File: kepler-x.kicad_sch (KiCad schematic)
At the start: 108 parts, among them IC1 SLG46826G, J1 HDMI_C_1.3, J2 Conn_01x02_Male, J3 MIDI OUT, J4 RasPI_IO_Header_B+, J5 AudioJack3, J6 MIDI IN, J7 Conn_01x02_Male, J8 Conn_02x07_Odd_Even, J9 Conn_01x02_Male, Q1 Q_PNP_BEC, Q2 Q_PNP_BEC, Q3 Q_NPN_BEC, Q4 Q_NPN_BEC, Q5 Q_NPN_BEC, Q6 Q_NPN_BEC, SW1 SWITCH_INV, SW2 SWITCH_INV, U1 Bus-X68000-ext, U10 74LVTH162245, U11 WM8804GEDS{slash}RV, U12 TC7MPB9307F, U13 TC7MPB9307F, U14 P0082(DE0-NANO), U15 PLR135-T10, U16 PCM5102, U17 LM1117GS-3.3, U18 H11L1, U2 LM1117GS-3.3, U3 INA3221, U4 74AHC16374, U5 74AHC16374, U6 74AHC16374, U7 74AHC16374, U8 74AHC16374, U9 74AHC16374, X1 ASV-24.576MHz, Y1 12MHz

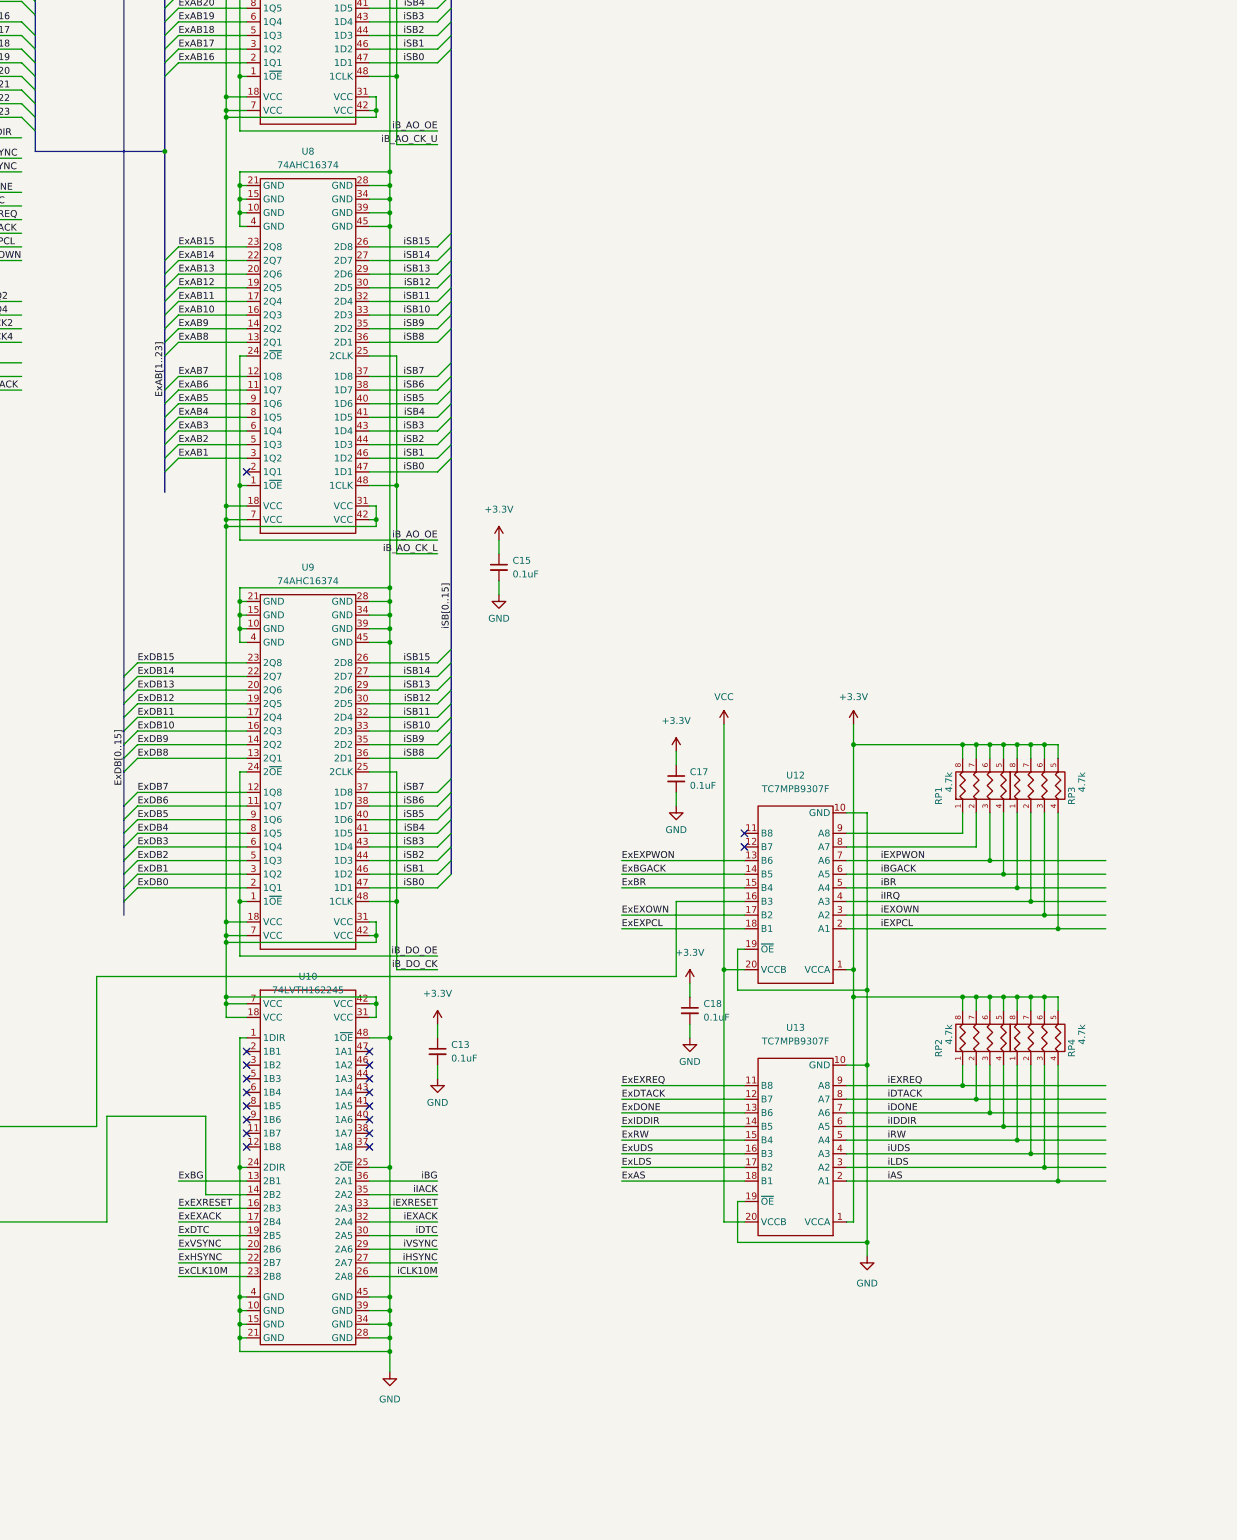
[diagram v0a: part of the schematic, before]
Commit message: Fixed the board can accept TC7MPB9307FT or TC7MPB9307FK.
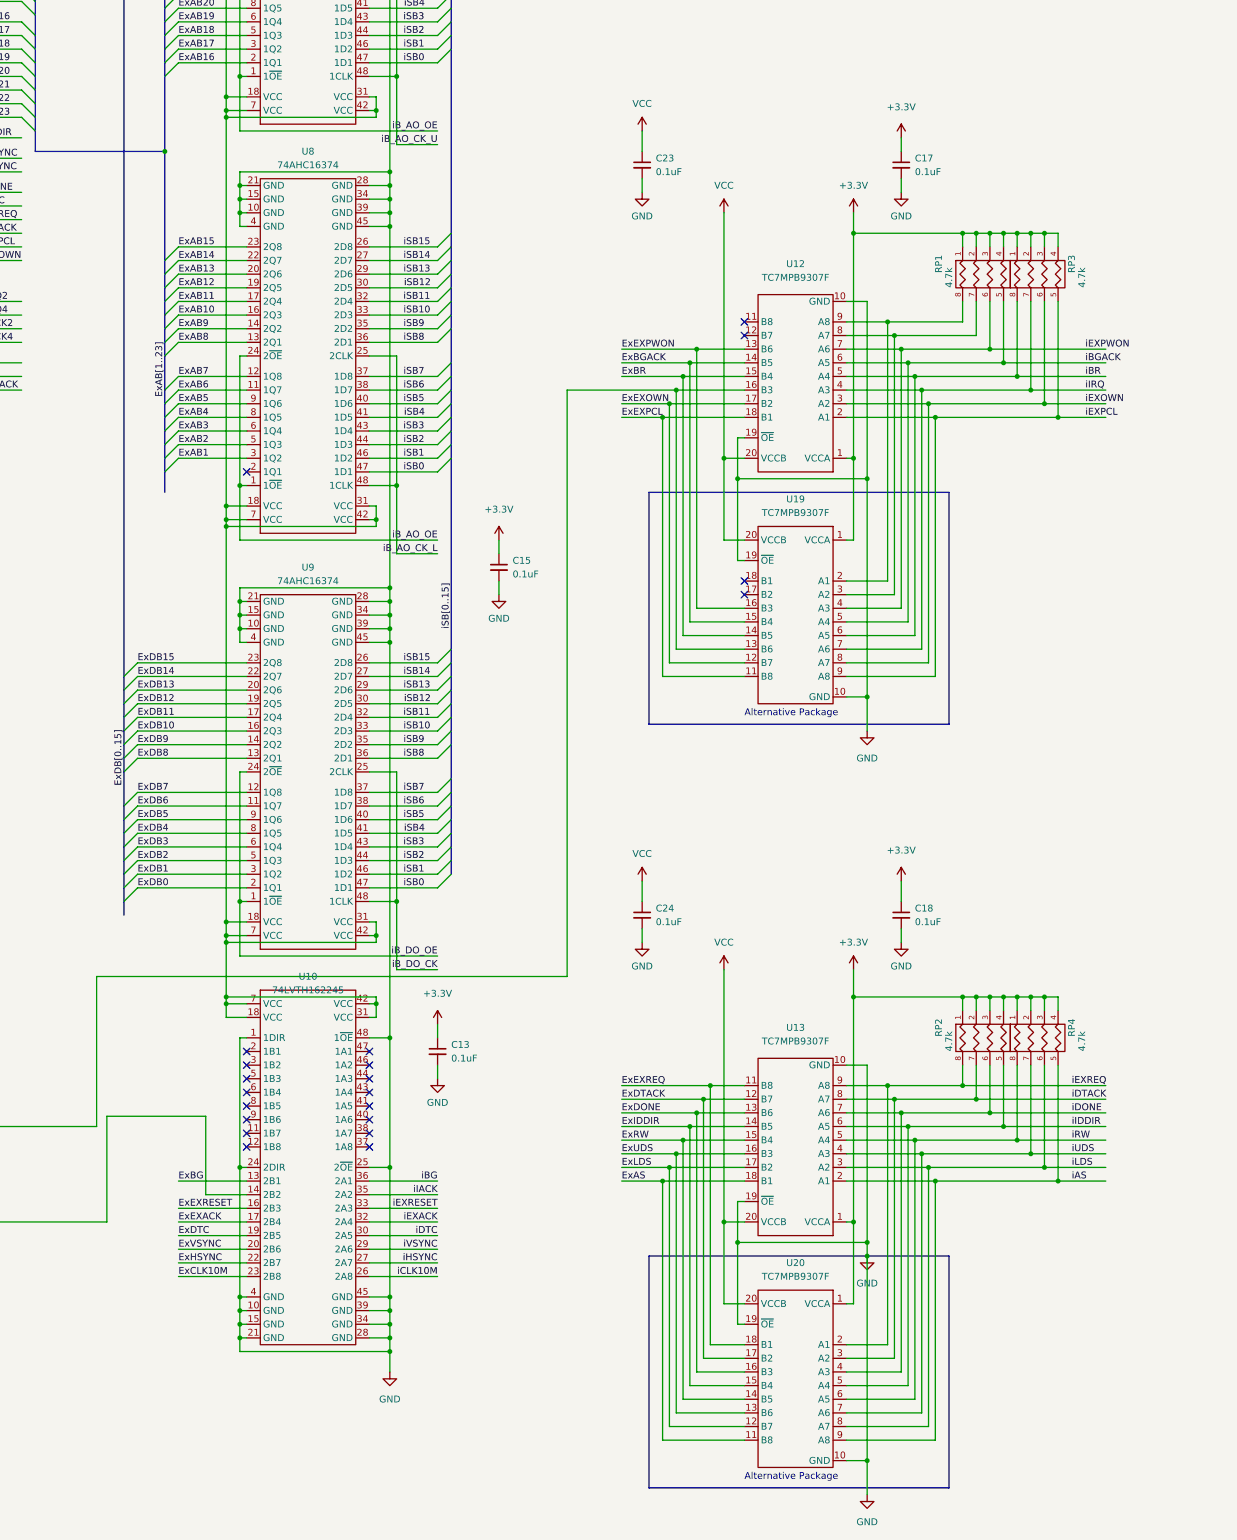
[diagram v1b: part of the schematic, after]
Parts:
- added C23, C24: 0.1uF, Capacitor_SMD:C_0603_1608Metric_Pad1.08x0.95mm_HandSolder, symbol Device:C_Small
- added U19, U20: TC7MPB9307F, x68000-ext:VSSOP-20_3x5mm_P0.5mm, symbol x68000-ext:TC7MPB9307F
- U12, U13: footprint Housings_SSOP:TSSOP-20_4.4x6.5mm_Pitch0.65mm -> x68000-ext:TSSOP-20_4.4x6.5mm_Pitch0.65mm
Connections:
- net +3V3: now also RP1.1 (P1), RP1.2 (P2), RP1.3 (P3), RP1.4 (P4), RP2.1 (P1), RP2.2 (P2), RP2.3 (P3), RP2.4 (P4), RP3.1 (P1), RP3.2 (P2), RP3.3 (P3), RP3.4 (P4), RP4.1 (P1), RP4.2 (P2), RP4.3 (P3), RP4.4 (P4), U19.1 (VCCA), U20.1 (VCCA); no longer RP1.5 (R4), RP1.6 (R3), RP1.7 (R2), RP1.8 (R1), RP2.5 (R4), RP2.6 (R3), RP2.7 (R2), RP2.8 (R1), RP3.5 (R4), RP3.6 (R3), RP3.7 (R2), RP3.8 (R1), RP4.5 (R4), RP4.6 (R3), RP4.7 (R2), RP4.8 (R1)
- net ExAS: now also U20.11 (B8)
- net ExBGACK: now also U19.15 (B4)
- net ExBR: now also U19.14 (B5)
- net ExDONE: now also U20.16 (B3)
- net ExDTACK: now also U20.17 (B2)
- net ExEXOWN: now also U19.12 (B7)
- net ExEXPCL: now also U19.11 (B8)
- net ExEXPWON: now also U19.16 (B3)
- net ExEXREQ: now also U20.18 (B1)
- net ExIDDIR: now also U20.15 (B4)
- net ExLDS: now also U20.12 (B7)
- net ExRW: now also U20.14 (B5)
- net ExUDS: now also U20.13 (B6)
- net GND: now also C23.2, C24.2, U19.10 (GND), U19.19 (~{OE}), U20.10 (GND), U20.19 (~{OE})
- net VCC: now also C23.1, C24.1, U19.20 (VCCB), U20.20 (VCCB)
- net iAS: now also RP4.5 (R4), U20.9 (A8); no longer RP4.4 (P4)
- net iBGACK: now also RP1.5 (R4), U19.5 (A4); no longer RP1.4 (P4)
- net iBR: now also RP3.8 (R1), U19.6 (A5); no longer RP3.1 (P1)
- net iDONE: now also RP2.6 (R3), U20.4 (A3); no longer RP2.3 (P3)
- net iDTACK: now also RP2.7 (R2), U20.3 (A2); no longer RP2.2 (P2)
- net iEXOWN: now also RP3.6 (R3), U19.8 (A7); no longer RP3.3 (P3)
- net iEXPCL: now also RP3.5 (R4), U19.9 (A8); no longer RP3.4 (P4)
- net iEXPWON: now also RP1.6 (R3), U19.4 (A3); no longer RP1.3 (P3)
- net iEXREQ: now also RP2.8 (R1), U20.2 (A1); no longer RP2.1 (P1)
- net iIDDIR: now also RP2.5 (R4), U20.5 (A4); no longer RP2.4 (P4)
- net iIRQ: now also RP3.7 (R2), U19.7 (A6); no longer RP3.2 (P2)
- net iLDS: now also RP4.6 (R3), U20.8 (A7); no longer RP4.3 (P3)
- net iRW: now also RP4.8 (R1), U20.6 (A5); no longer RP4.1 (P1)
- net iUDS: now also RP4.7 (R2), U20.7 (A6); no longer RP4.2 (P2)
- net at U12.9 (A8): now also RP1.8 (R1), U19.2 (A1); no longer RP1.1 (P1)
- net at U12.8 (A7): now also RP1.7 (R2), U19.3 (A2); no longer RP1.2 (P2)
- net at SW1.2, U12.16 (B3): now also U19.13 (B6)
- no-connect marks 59 -> 61
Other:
- note added: "Alternative Package"
- moved on the sheet: C17, C18, RP1, RP3, U12

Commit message: Commit current status
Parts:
- added C?: 0.1uF, Capacitor_SMD:C_0603_1608Metric_Pad1.08x0.95mm_HandSolder, symbol Device:C_Small
- added C?: 0.01uF, Capacitor_SMD:C_0603_1608Metric_Pad1.08x0.95mm_HandSolder, symbol Device:C_Small
- added FB? (x2): FerriteBead_Small, symbol Device:FerriteBead_Small
- added JP? (x10): Jumper_NO_Small, symbol device:Jumper_NO_Small
- added SW?: SWITCH_INV, Pin_Headers:Pin_Header_Straight_1x03, symbol device:SWITCH_INV
- R10, R11: value R_Small_US -> 10K
- R12, R13: value R_Small_US -> 110
- R14: value R_Small_US -> 2.2K
- R15: value R_Small_US -> 120
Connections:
- net +3V3: now also SW?.3; no longer X1.4 (Vdd)
- net FM_CLK4M: now also JP?.1; no longer J4.26 (GPIO7/CE1-N)
- net FM_DAT: now also JP?.1; no longer J4.32 (GPIO12)
- net FM_IRQ: now also JP?.1; no longer J4.29 (GPIO5)
- net FM_LRCK: now also JP?.1; no longer J4.33 (GPIO13)
- net FM_PHY: now also JP?.1; no longer J4.31 (GPIO6)
- net FM_RD: now also JP?.1; no longer J4.27 (ID_SD)
- net FM_SCLK: now also JP?.1; no longer J4.36 (GPIO16)
- net FM_SDATA: now also JP?.1; no longer J4.37 (GPIO26)
- net FM_WR: now also JP?.1; no longer J4.28 (ID_SC)
- net GND: now also C?.2, C?.2; no longer J4.17 (3V3)
- net iCLK24M576: now also FB?.2; no longer X1.3 (OUT)
- net iEXRESET: now also JP?.1; no longer J4.40 (GPIO21)
- net at D10.2 (A2), D7.2 (A): now also J3.T; no longer J3.R
- net at D10.1 (A1), D6.1 (K): now also J3.R; no longer J3.T
- net at D8.1 (A1), Q5.2 (E), R15.2: now also J6.T; no longer J6.R
- net at D8.2 (A2), D9.2 (A): now also J6.R; no longer J6.T
- net at U14.JP2_29 (GPIO-1_VCC3P3): now also SW?.1
- new net: J4.31 (GPIO6), JP?.2
- new net: FB?.1, X1.3 (OUT)
- new net: C?.1, C?.1, FB?.2, X1.4 (Vdd)
- new net: J4.37 (GPIO26), JP?.2
- new net: J4.32 (GPIO12), JP?.2
- new net: J4.28 (ID_SC), JP?.2
- new net: FB?.1, SW?.2
- new net: J4.29 (GPIO5), JP?.2
- new net: J4.33 (GPIO13), JP?.2
- new net: J4.26 (GPIO7/CE1-N), JP?.2
- new net: J4.40 (GPIO21), JP?.2
- new net: J4.27 (ID_SD), JP?.2
- new net: J4.36 (GPIO16), JP?.2
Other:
- moved on the sheet: J3, TP4
